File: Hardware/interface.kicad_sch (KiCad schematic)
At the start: 1 part

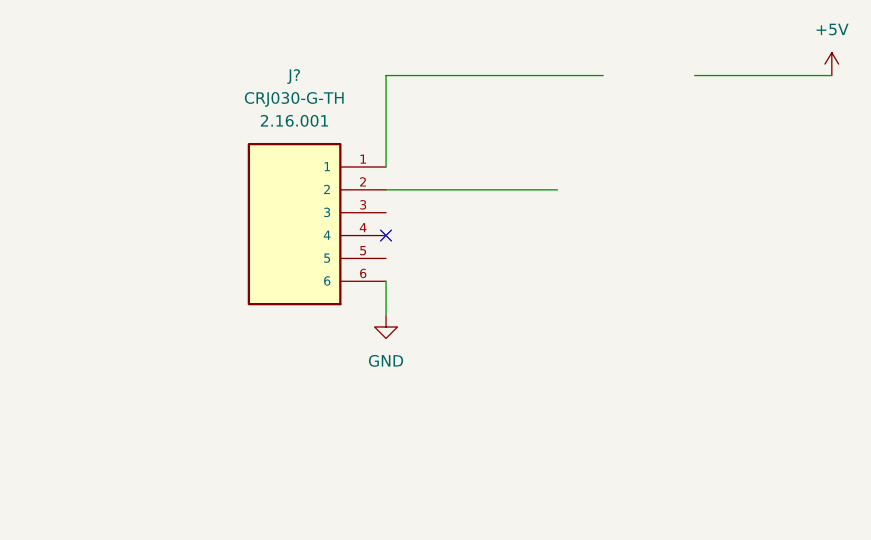
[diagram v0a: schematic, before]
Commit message: Rebuild p1_reader project
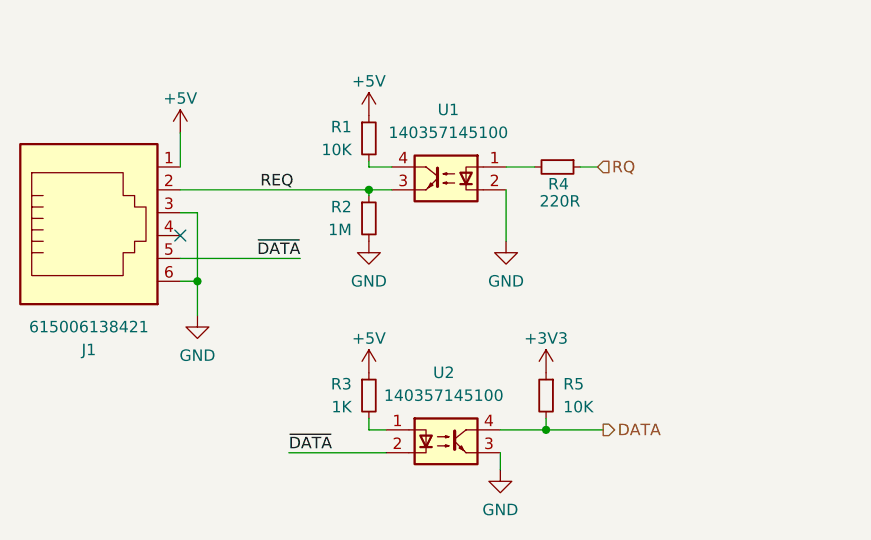
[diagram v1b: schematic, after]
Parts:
- removed J?: CRJ030-G-TH, CUI_CRJ030-G-TH, symbol mt_lib:CRJ030-G-TH
- added J1: 615006138421, manul_tech:615006138421, symbol manul_tech:615006138421
- added R1, R5: 10K, Resistor_SMD:R_0402_1005Metric, symbol Device:R_Small
- added R2: 1M, Resistor_SMD:R_0402_1005Metric, symbol Device:R_Small
- added R3: 1K, Resistor_SMD:R_0402_1005Metric, symbol Device:R_Small
- added R4: 220R, Resistor_SMD:R_0402_1005Metric, symbol Device:R_Small
- added U1, U2: 140357145100, symbol manul_tech:140357145100
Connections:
- net +5V: now also J1.1, R1.1, R3.1
- net GND: now also J1.3, J1.6, R2.2, U1.2, U2.3
- new net: R4.2, U1.1
- new net: R3.2, U2.1
- new net: R1.2, U1.4
- new net +3V3: R5.1
- new net DATA: R5.2, U2.4
- new net REQ: J1.2, R2.1, U1.3
- new net RQ: R4.1
- new net ~{DATA}: J1.5, U2.2

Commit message: Schematic completed, started placing
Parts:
- U1, U2: footprint (none) -> Package_SO:SOP-4_3.8x4.1mm_P2.54mm
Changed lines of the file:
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@@
       (effects (font (size 1.27 1.27)))
     )
-    (property "Footprint" "" (at 106.68 45.72 0)
+    (property "Footprint" "Package_SO:SOP-4_3.8x4.1mm_P2.54mm" (at 106.68 45.72 0)
       (effects (font (size 1.27 1.27) italic) (justify left) hide)
     )
@@
         (path "/d9bd008b-84e8-4d0b-9177-df1b9a254894/7d5948d1-8ff5-41bc-bc50-eec041142a58"
           (reference "R2") (unit 1)
+        )
+      )
+    )
+  )
+  (symbol (lib_id "manul_tech:140357145100") (at 102.235 69.85 0) (unit 1)
+    (in_bom yes) (on_board yes) (dnp no)
+    (property "Reference" "U2" (at 101.6635 62.23 0)
+      (effects (font (size 1.27 1.27)))
+    )
+    (property "Value" "140357145100" (at 101.6635 64.77 0)
+      (effects (font (size 1.27 1.27)))
+    )
+    (property "Footprint" "Package_SO:SOP-4_3.8x4.1mm_P2.54mm" (at 97.155 74.93 0)
+      (effects (font (size 1.27 1.27) italic) (justify left) hide)
+    )
+    (property "Datasheet" "" (at 101.6 69.85 0)
+      (effects (font (size 1.27 1.27)) (justify left) hide)
+    )
+    (pin "1")
+    (pin "2")
+    (pin "3")
+    (pin "4")
+    (instances
+      (project "sp1_communicator"
+        (path "/d9bd008b-84e8-4d0b-9177-df1b9a254894/7d5948d1-8ff5-41bc-bc50-eec041142a58"
+          (reference "U2") (unit 1)
         )
       )
@@
         )
       )
-    )
-  )
-  (symbol (lib_id "manul_tech:140357145100") (at 102.235 69.85 0) (unit 1)
-    (in_bom yes) (on_board yes) (dnp no)
-    (property "Reference" "U2" (at 101.6635 62.23 0)
-      (effects (font (size 1.27 1.27)))
-    )
-    (property "Value" "140357145100" (at 101.6635 64.77 0)
-      (effects (font (size 1.27 1.27)))
-    )
-    (property "Footprint" "" (at 97.155 74.93 0)
-      (effects (font (size 1.27 1.27) italic) (justify left) hide)
-    )
-    (property "Datasheet" "" (at 101.6 69.85 0)
-      (effects (font (size 1.27 1.27)) (justify left) hide)
-    )
-    (pin "1")
-    (pin "2")
-    (pin "3")
-    (pin "4")
-    (instances
-      (project "sp1_communicator"
-        (path "/d9bd008b-84e8-4d0b-9177-df1b9a254894/7d5948d1-8ff5-41bc-bc50-eec041142a58"
-          (reference "U2") (unit 1)
-        )
-      )

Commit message: completed routing
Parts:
- removed J1: 615006138421, manul_tech:615006138421, symbol manul_tech:615006138421
- removed R1, R5: 10K, Resistor_SMD:R_0402_1005Metric, symbol Device:R_Small
- removed R2: 1M, Resistor_SMD:R_0402_1005Metric, symbol Device:R_Small
- removed R3: 1K, Resistor_SMD:R_0402_1005Metric, symbol Device:R_Small
- removed R4: 220R, Resistor_SMD:R_0402_1005Metric, symbol Device:R_Small
- removed U1, U2: 140357145100, Package_SO:SOP-4_3.8x4.1mm_P2.54mm, symbol manul_tech:140357145100
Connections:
- no-connect marks 1 -> 0
